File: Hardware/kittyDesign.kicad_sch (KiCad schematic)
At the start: 0 parts

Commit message: featÑ add routes
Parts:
- added BT1: Battery_Cell, footprints:BAT-HLD-001, symbol Device:Battery_Cell
- added C1: 0.1uF, Capacitor_SMD:C_0805_2012Metric, symbol Device:C_Small
- added D1: Blue, LED_SMD:LED_0805_2012Metric, symbol Device:LED_Small
- added D2: Green, LED_SMD:LED_0805_2012Metric, symbol Device:LED_Small
- added D3: Yellow, LED_SMD:LED_0805_2012Metric, symbol Device:LED_Small
- added D4: Red, LED_SMD:LED_0805_2012Metric, symbol Device:LED_Small
- added D5: Orange, LED_SMD:LED_0805_2012Metric, symbol Device:LED_Small
- added J1: Conn_01x04_Socket, Connector_PinHeader_2.54mm:PinHeader_1x04_P2.54mm_Vertical, symbol Connector:Conn_01x04_Socket
- added R1, R2, R3, R4, R5: 330R, Resistor_SMD:R_0805_2012Metric, symbol Device:R_Small
- added SW2: On, footprints:MSK12C02, symbol Switch:SW_DPDT_x2
- added U1: PY32F002AA15M6TU, footprints:PY32F002AA15M, symbol MCU_PY32F002:PY32F002AA15M6TU
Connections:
- new net: D4.2 (A), R3.1
- new net: D2.2 (A), R1.1
- new net: D5.2 (A), R5.1
- new net: BT1.1 (-), SW2.2 (B)
- new net: D1.2 (A), R4.1
- new net: D3.2 (A), R2.1
- new net +3.3V: BT1.2 (+), C1.1, J1.1 (Pin_1), U1.1 (VCC)
- new net GND: C1.2, D1.1 (K), D2.1 (K), D3.1 (K), D4.1 (K), D5.1 (K), J1.4 (Pin_4), SW2.1 (A), SW2.4 (C), U1.10 (GND)
- new net PA1: R5.2, U1.5 (PA1)
- new net PA5: R2.2, U1.3 (PA5/PF1-OSCOUT)
- new net PA6: R1.2, U1.6 (PA6)
- new net PA7: R4.2, U1.7 (PA7)
- new net PF0: R3.2, U1.2 (PF0-OSCIN)
- new net SWCLK: J1.2 (Pin_2), U1.9 (PA14-SWC/PB3)
- new net SWDIO: J1.3 (Pin_3), U1.8 (PA13-SWD)
- no-connect marks 0 -> 2
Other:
- note added: "Battery"
- note added: "LED"
- note added: "Microcontroller"

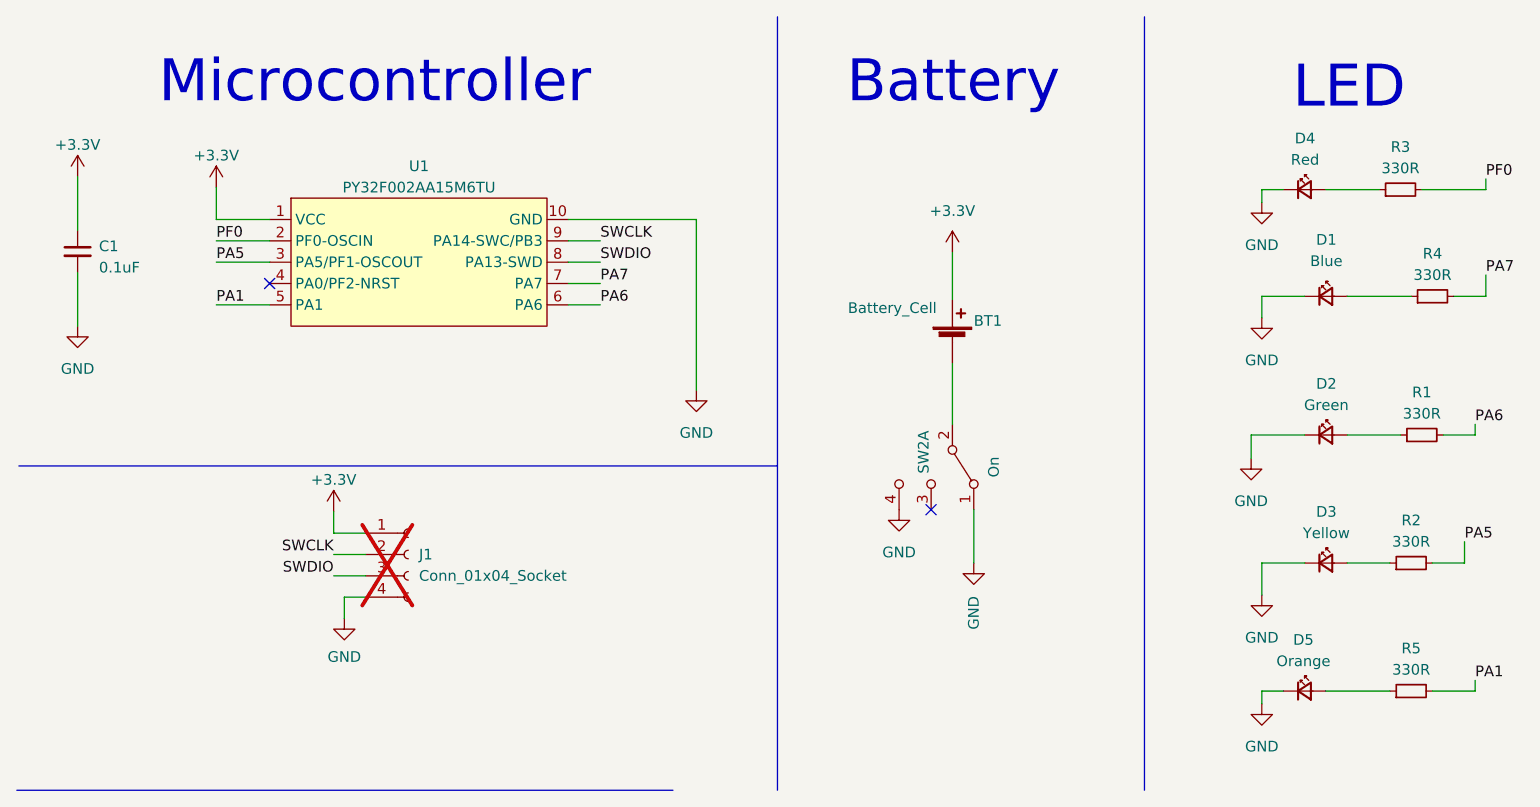
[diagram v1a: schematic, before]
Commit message: refactor: change MCU for a ch32v00x
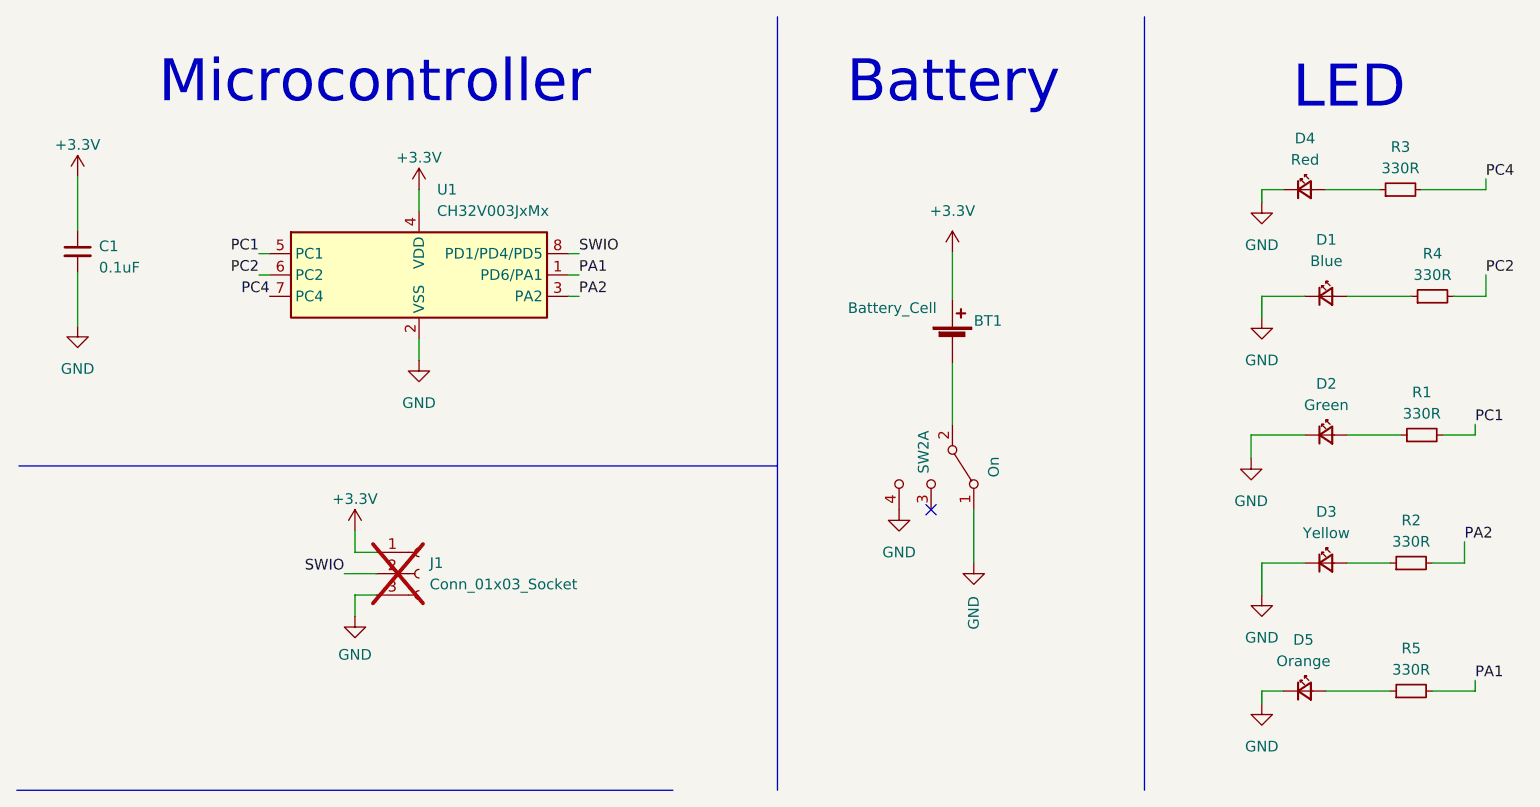
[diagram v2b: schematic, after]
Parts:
- removed J1: Conn_01x04_Socket, Connector_PinHeader_2.54mm:PinHeader_1x04_P2.54mm_Vertical, symbol Connector:Conn_01x04_Socket
- removed U1: PY32F002AA15M6TU, footprints:PY32F002AA15M, symbol MCU_PY32F002:PY32F002AA15M6TU
- added J1: Conn_01x03_Socket, Connector_PinHeader_2.54mm:PinHeader_1x03_P2.54mm_Vertical, symbol Connector:Conn_01x03_Socket
- added U1: CH32V003JxMx, Package_SO:JEITA_SOIC-8_3.9x4.9mm_P1.27mm, symbol MCU_WCH_CH32V0:CH32V003JxMx
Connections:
- net +3.3V: now also J1.1 (Pin_1), U1.4 (VDD)
- net GND: now also J1.3 (Pin_3), U1.2 (VSS)
- net PA1: now also U1.1 (PD6/PA1)
- net PA5 renamed PA2
- net PA2: now also U1.3 (PA2)
- net PA6 renamed PC1
- net PC1: now also U1.5 (PC1)
- net PA7 renamed PC2
- net PC2: now also U1.6 (PC2)
- net PF0 renamed PC4
- net PC4: now also U1.7 (PC4)
- new net SWIO: J1.2 (Pin_2), U1.8 (PD1/PD4/PD5)
- no-connect marks 2 -> 1
